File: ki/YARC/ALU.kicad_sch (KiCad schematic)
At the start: 7 parts, among them U116 AS6C6264, U117 AS6C6264, U118 AS6C6264, U119 74LS245, U120 74LS245, U121 74LS573, U122 74LS574

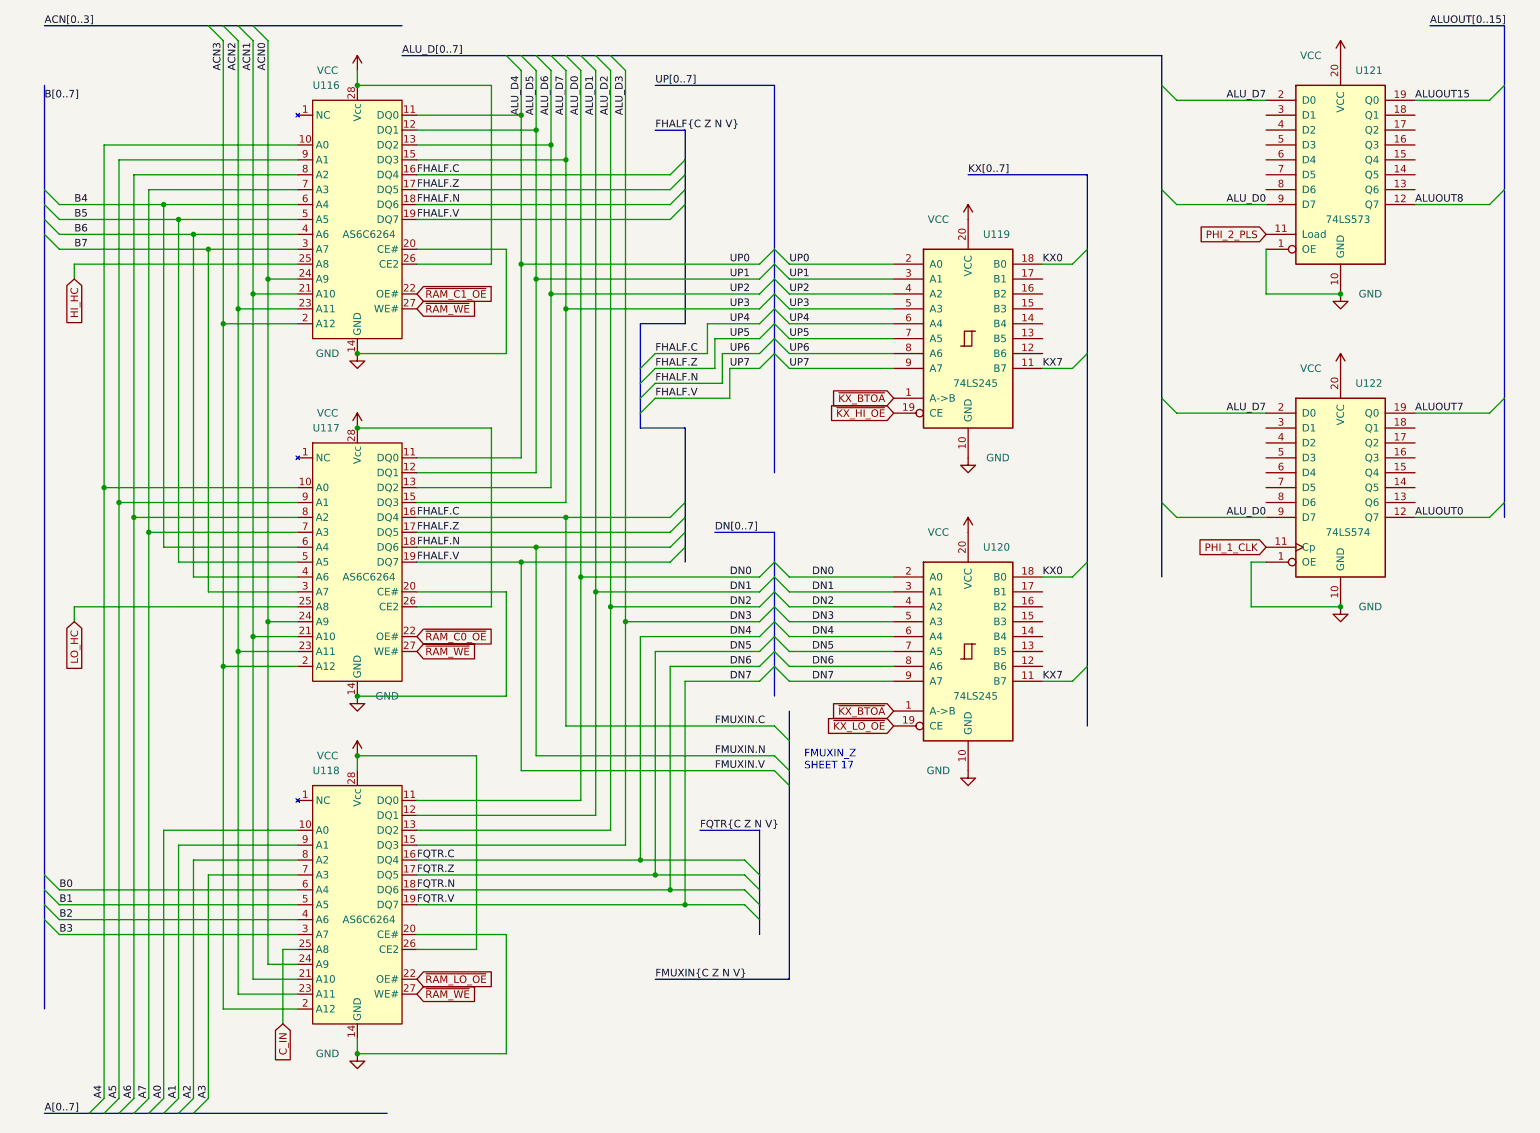
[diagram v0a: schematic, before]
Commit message: Removed about 2/3 of 2300+ errors from the ERC
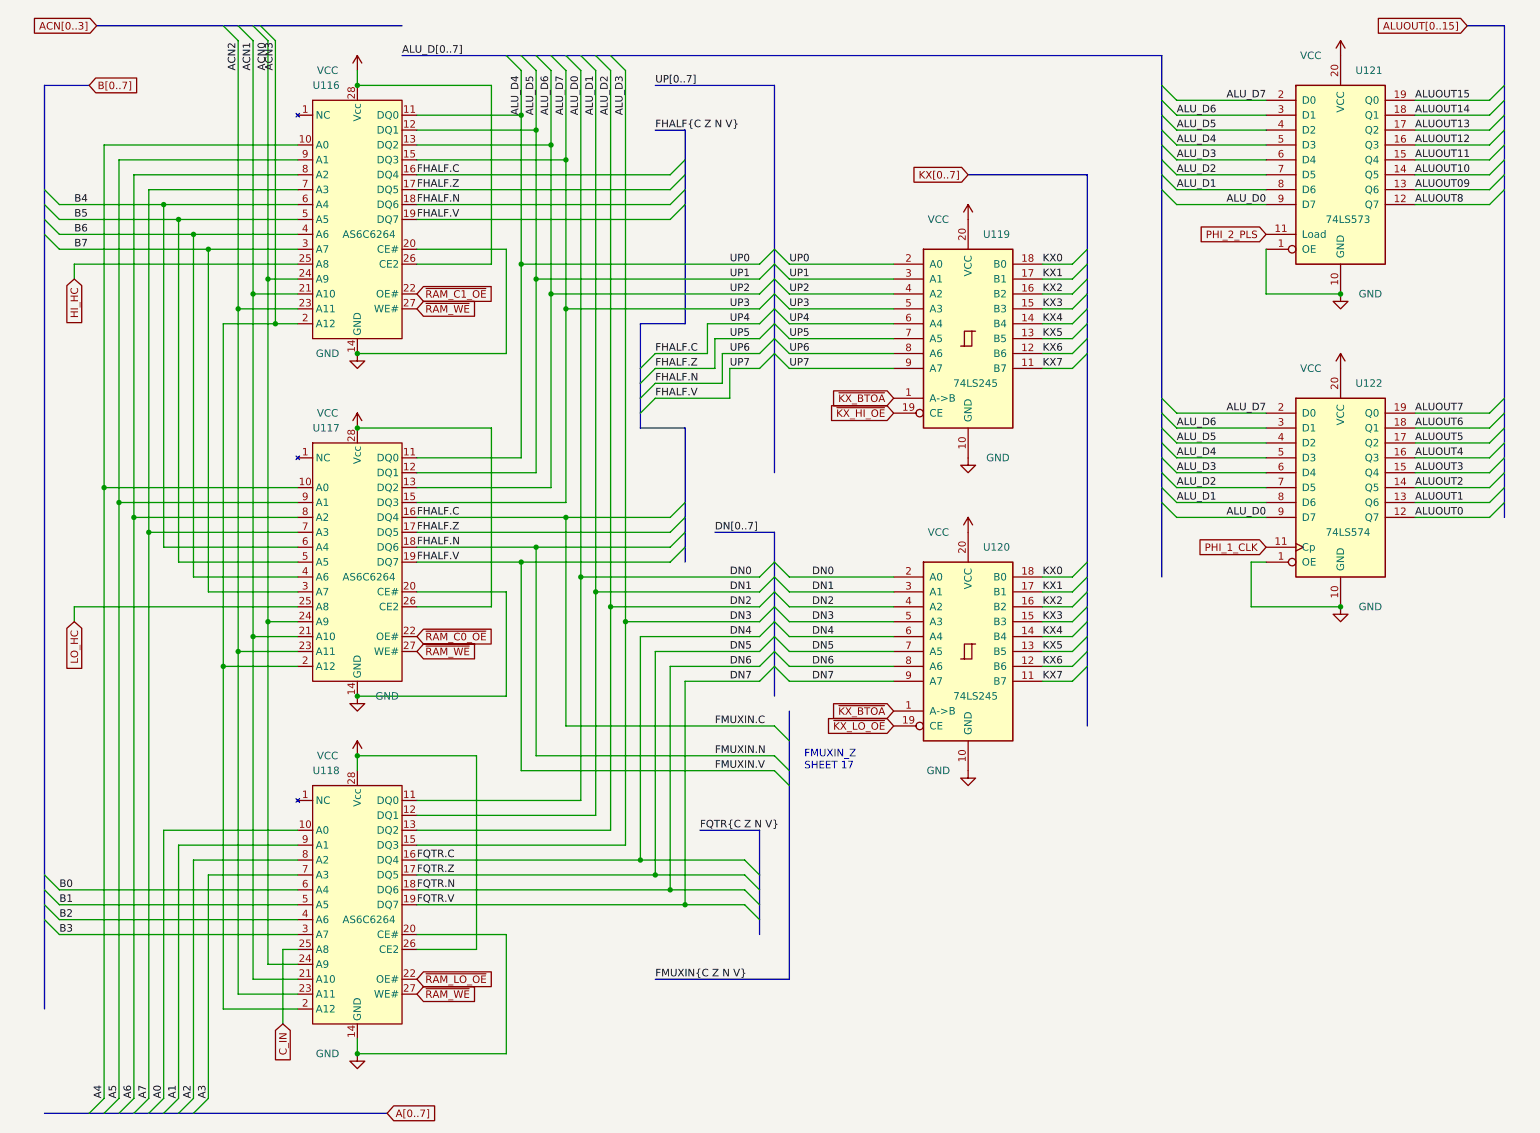
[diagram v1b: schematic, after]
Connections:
- net ALU_D1: now also U121.8 (D6), U122.8 (D6)
- net ALU_D2: now also U121.7 (D5), U122.7 (D5)
- net ALU_D3: now also U121.6 (D4), U122.6 (D4)
- net ALU_D4: now also U121.5 (D3), U122.5 (D3)
- net ALU_D5: now also U121.4 (D2), U122.4 (D2)
- net ALU_D6: now also U121.3 (D1), U122.3 (D1)
- net KX6: now reaches U120.12 (B6)
- net KX6: now also U119.12 (B6)
- net KX5: now reaches U120.13 (B5)
- net KX5: now also U119.13 (B5)
- net KX4: now reaches U120.14 (B4)
- net KX4: now also U119.14 (B4)
- net KX3: now reaches U120.15 (B3)
- net KX3: now also U119.15 (B3)
- net KX2: now reaches U120.16 (B2)
- net KX2: now also U119.16 (B2)
- net KX1: now reaches U120.17 (B1)
- net KX1: now also U119.17 (B1)
- net ALUOUT1: now reaches U122.13 (Q6)
- net ALUOUT2: now reaches U122.14 (Q5)
- net ALUOUT3: now reaches U122.15 (Q4)
- net ALUOUT4: now reaches U122.16 (Q3)
- net ALUOUT5: now reaches U122.17 (Q2)
- net ALUOUT6: now reaches U122.18 (Q1)
- net ALUOUT09: now reaches U121.13 (Q6)
- net ALUOUT10: now reaches U121.14 (Q5)
- net ALUOUT11: now reaches U121.15 (Q4)
- net ALUOUT12: now reaches U121.16 (Q3)
- net ALUOUT13: now reaches U121.17 (Q2)
- net ALUOUT14: now reaches U121.18 (Q1)

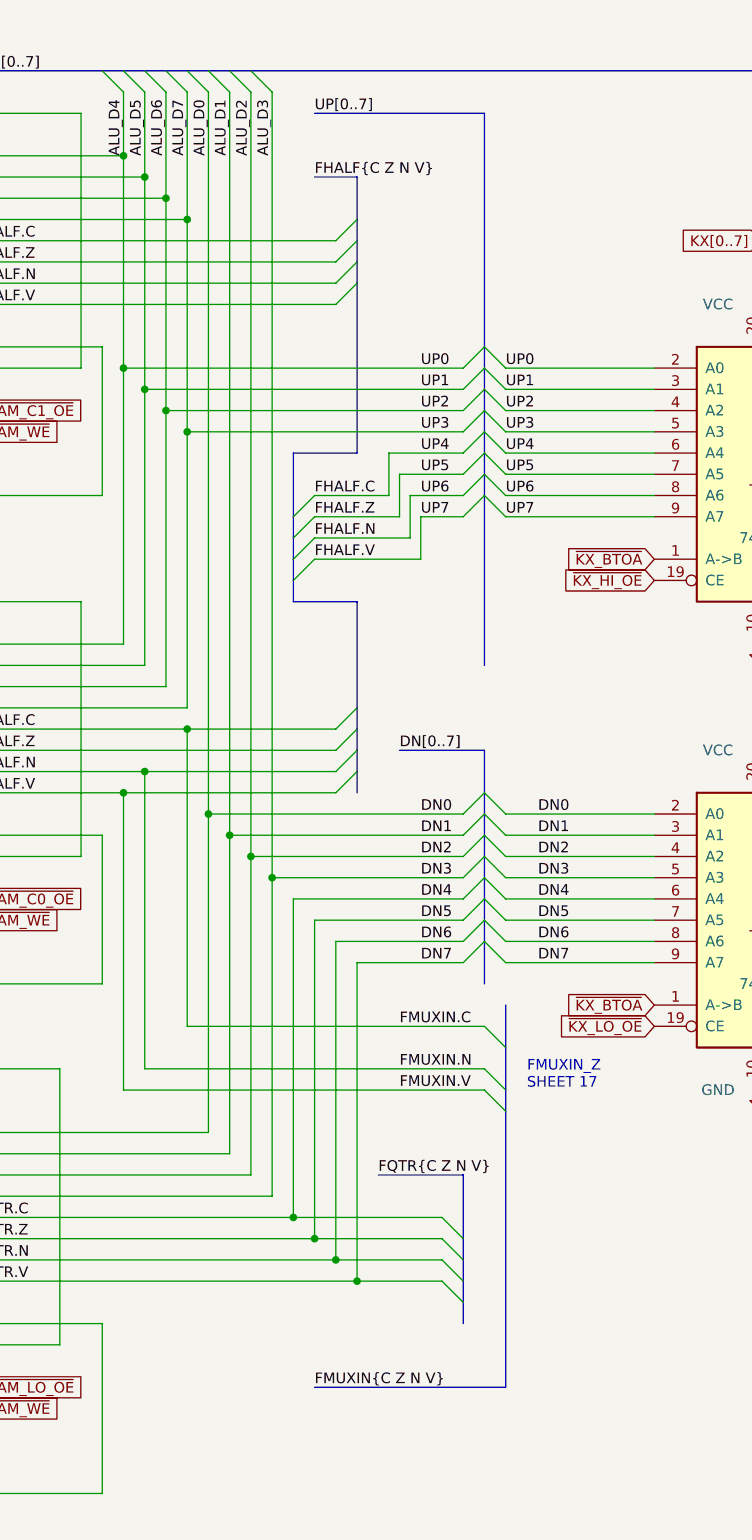
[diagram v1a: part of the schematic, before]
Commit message: Ongoing fixes for ERC errors
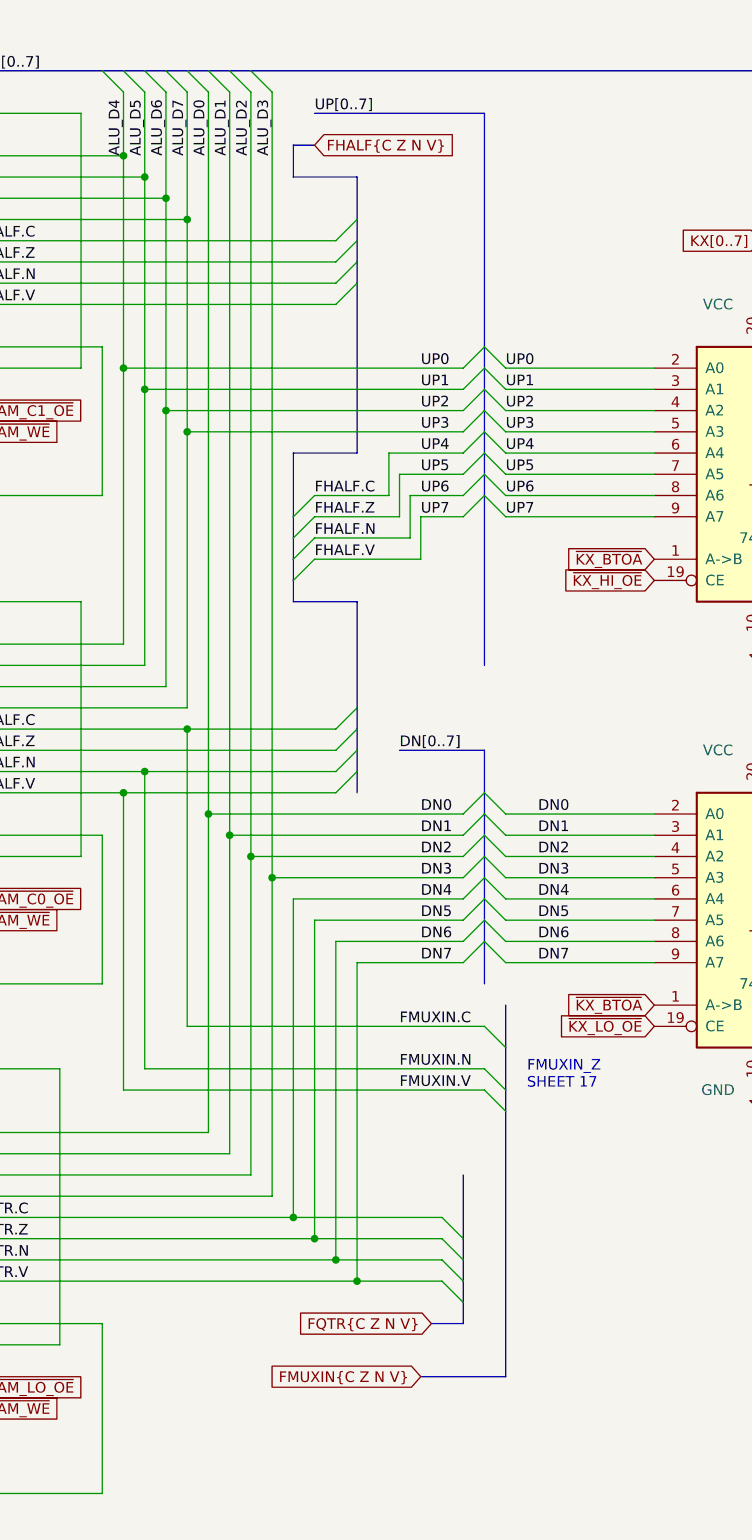
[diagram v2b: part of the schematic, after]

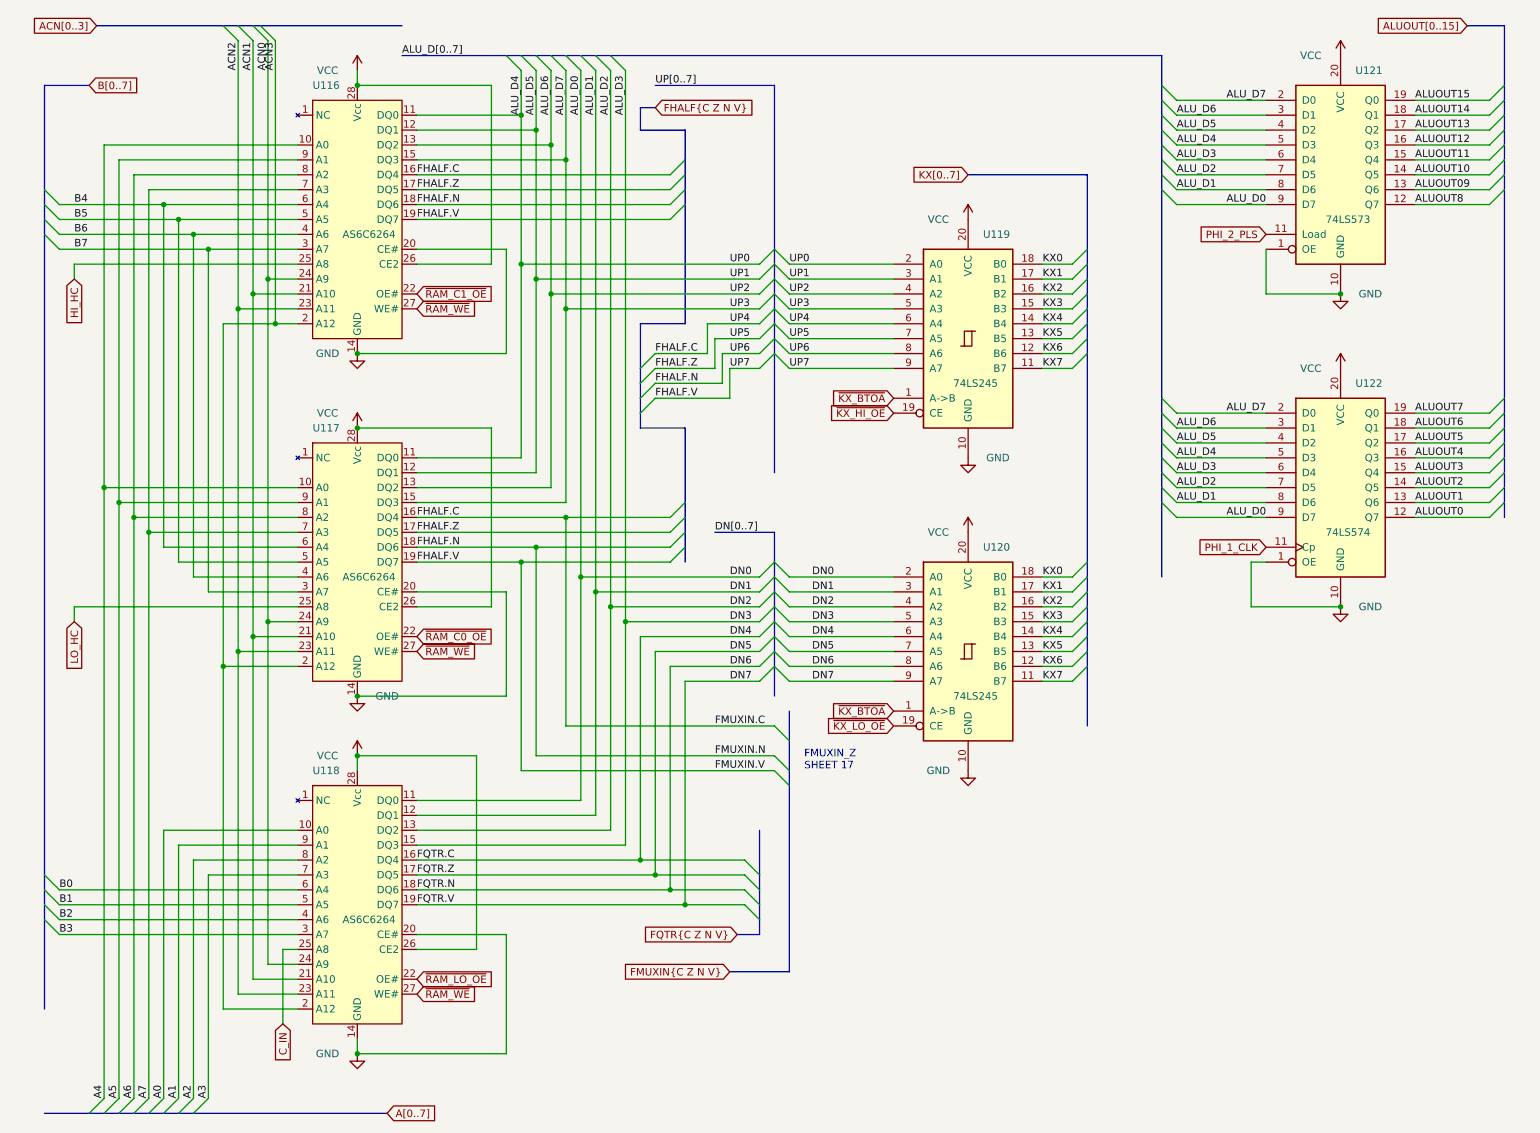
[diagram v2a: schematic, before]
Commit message: Schematic for addressing unit is complete and all ERC violations addressed
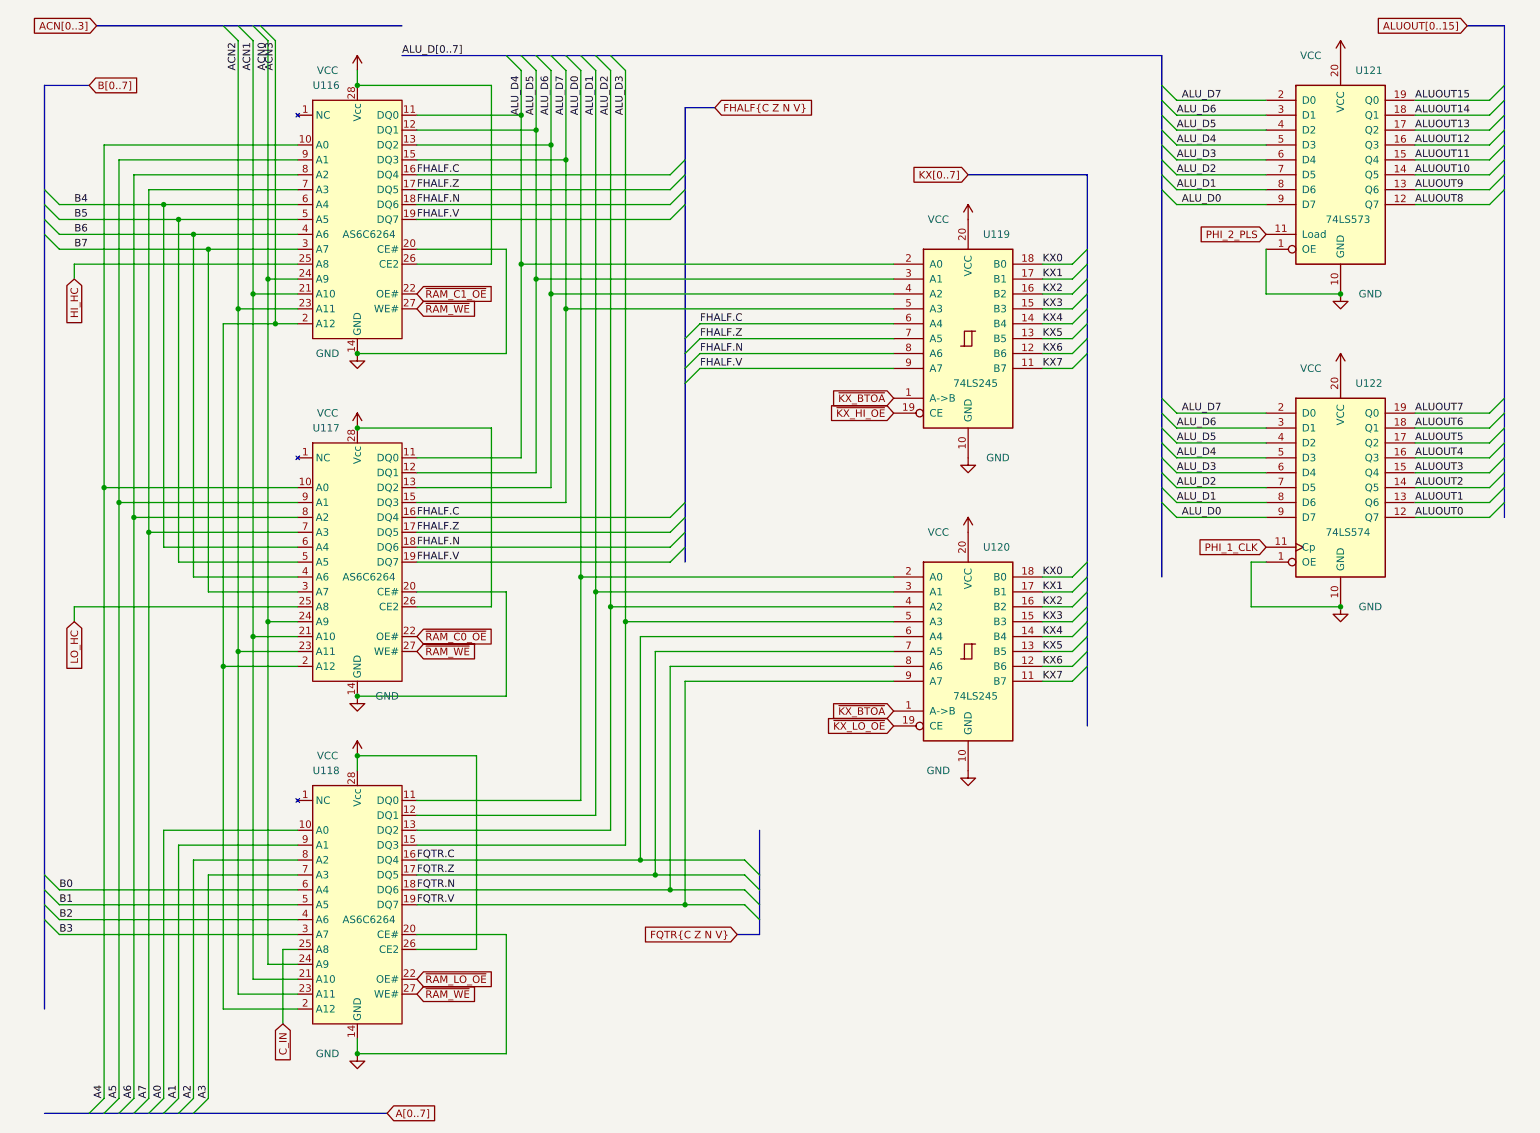
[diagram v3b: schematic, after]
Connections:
- net ALUOUT09 renamed ALUOUT9
- net DN4 renamed FQTR.C
- net DN5 renamed FQTR.Z
- net DN6 renamed FQTR.N
- net DN7 renamed FQTR.V
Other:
- note removed: "FMUXIN_Z SHEET 17"
